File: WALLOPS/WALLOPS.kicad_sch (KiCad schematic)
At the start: 17 parts, among them U9 TPS62147RGXR

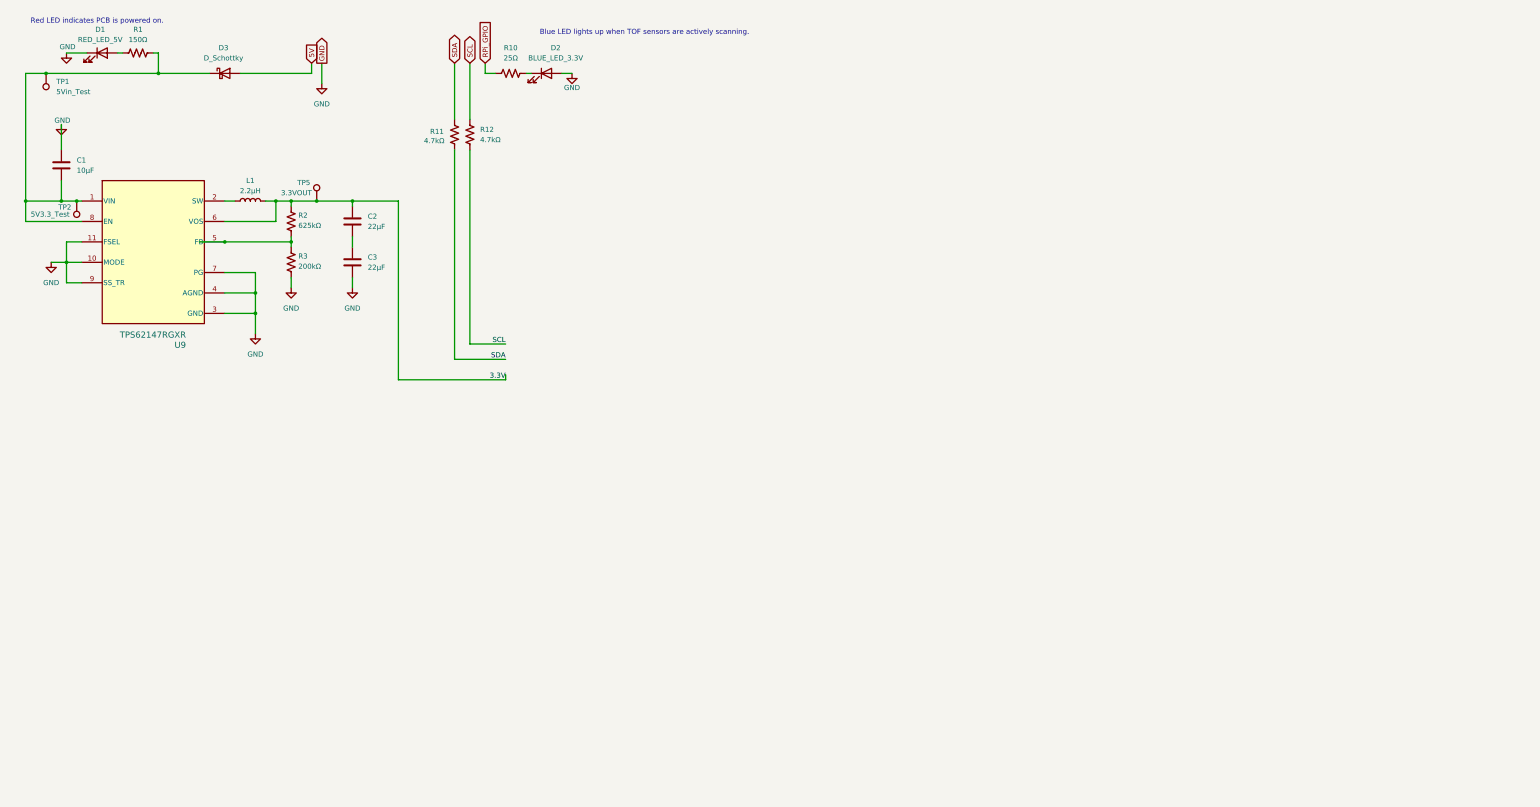
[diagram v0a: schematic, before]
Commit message: Added updated schematics for WALLOPS
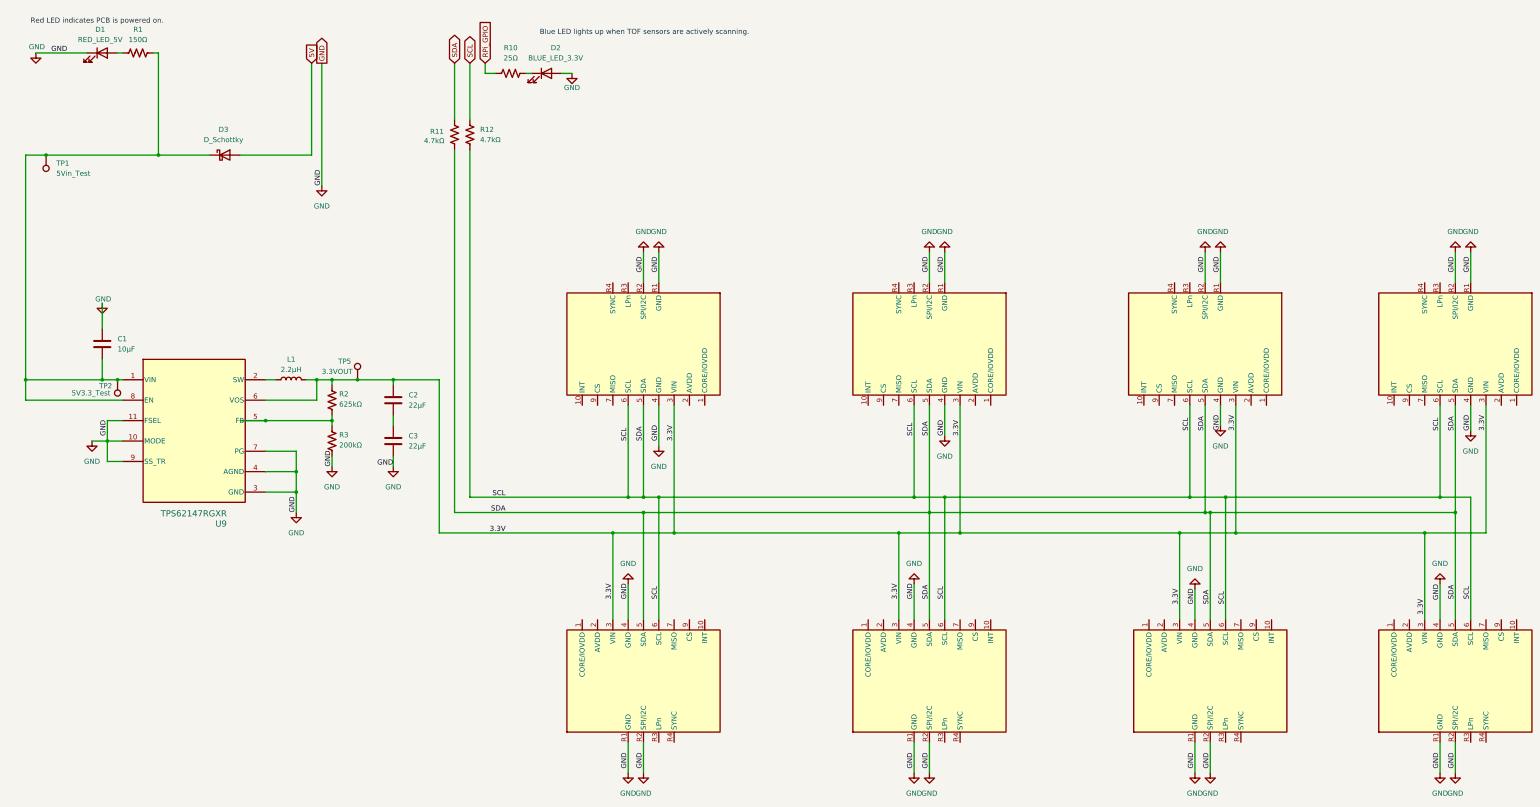
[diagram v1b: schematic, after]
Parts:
- added U1, U2, U3, U4, U5, U6, U7, U8: ~, symbol RockSat_Sym:VL53L8CX
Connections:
- net SDA is gone; now on net SCL: R11.1, R11.2
- net 3.3V: now also U1.3 (VIN), U2.3 (VIN), U3.3 (VIN), U4.3 (VIN), U5.3 (VIN), U6.3 (VIN), U7.3 (VIN), U8.3 (VIN)
- net GND: now also U1.4 (GND), U1.R1 (GND), U1.R2 (SPI/I2C), U2.4 (GND), U2.R1 (GND), U2.R2 (SPI/I2C), U3.4 (GND), U3.R1 (GND), U3.R2 (SPI/I2C), U4.4 (GND), U4.R1 (GND), U4.R2 (SPI/I2C), U5.4 (GND), U5.R1 (GND), U5.R2 (SPI/I2C), U6.4 (GND), U6.R1 (GND), U6.R2 (SPI/I2C), U7.4 (GND), U7.R1 (GND), U7.R2 (SPI/I2C), U8.4 (GND), U8.R1 (GND), U8.R2 (SPI/I2C)
- net SCL: now also U1.5 (SDA), U1.6 (SCL), U2.5 (SDA), U2.6 (SCL), U3.5 (SDA), U3.6 (SCL), U4.5 (SDA), U4.6 (SCL), U5.5 (SDA), U5.6 (SCL), U6.5 (SDA), U6.6 (SCL), U7.5 (SDA), U7.6 (SCL), U8.5 (SDA), U8.6 (SCL)
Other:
- moved on the sheet: C1, C2, C3, D3, L1, R2, R3, TP1, TP2, TP5, U9

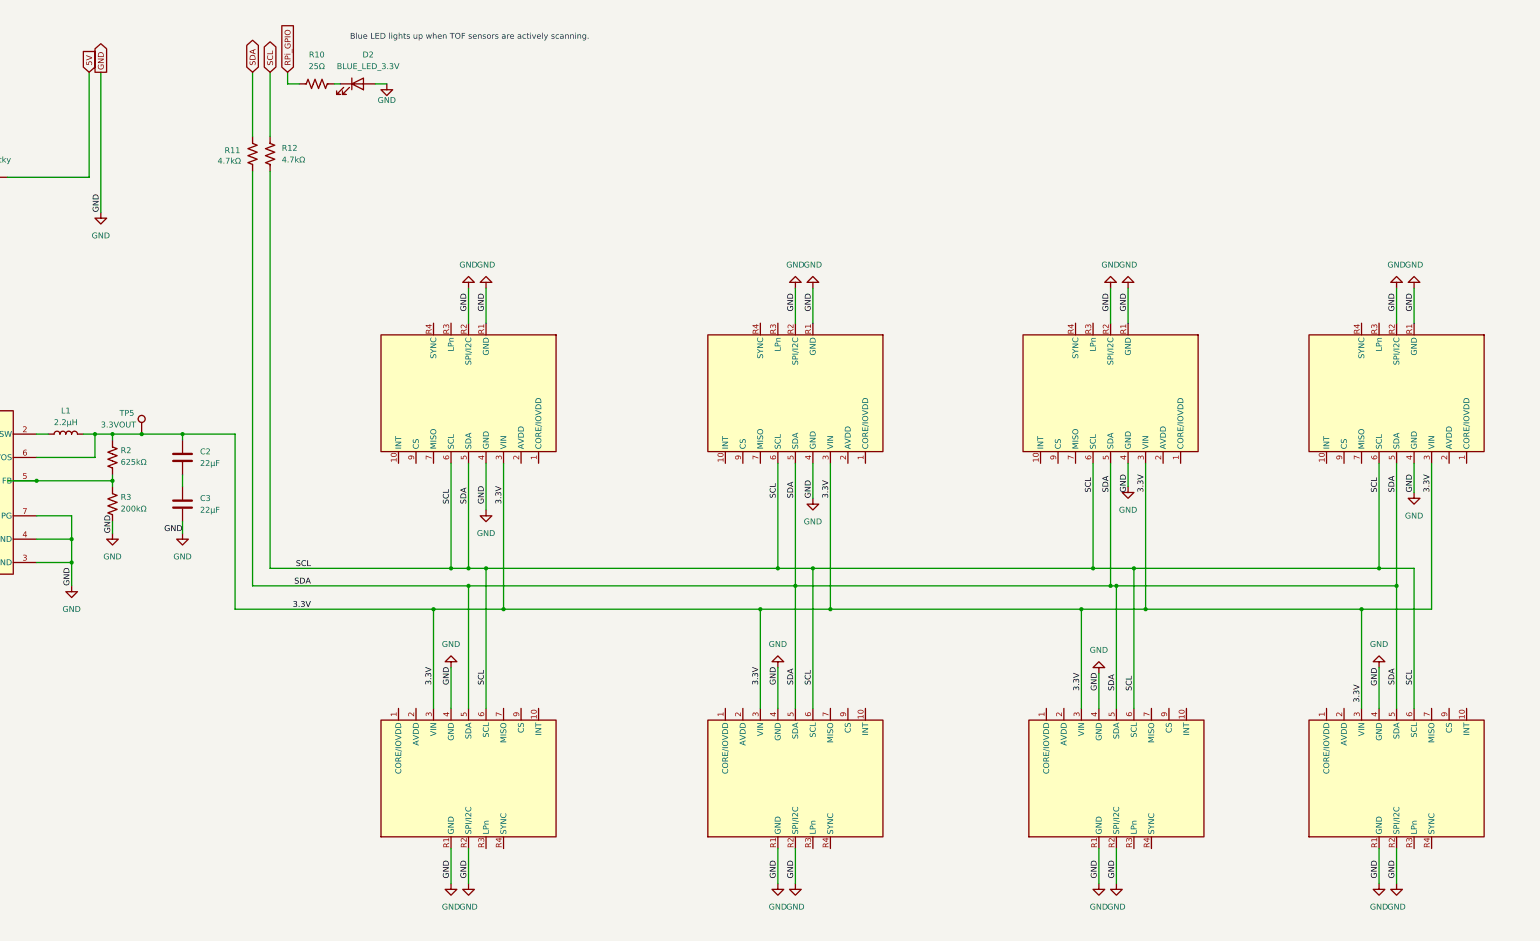
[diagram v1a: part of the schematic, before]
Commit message: Hooked up AVDD to LPn
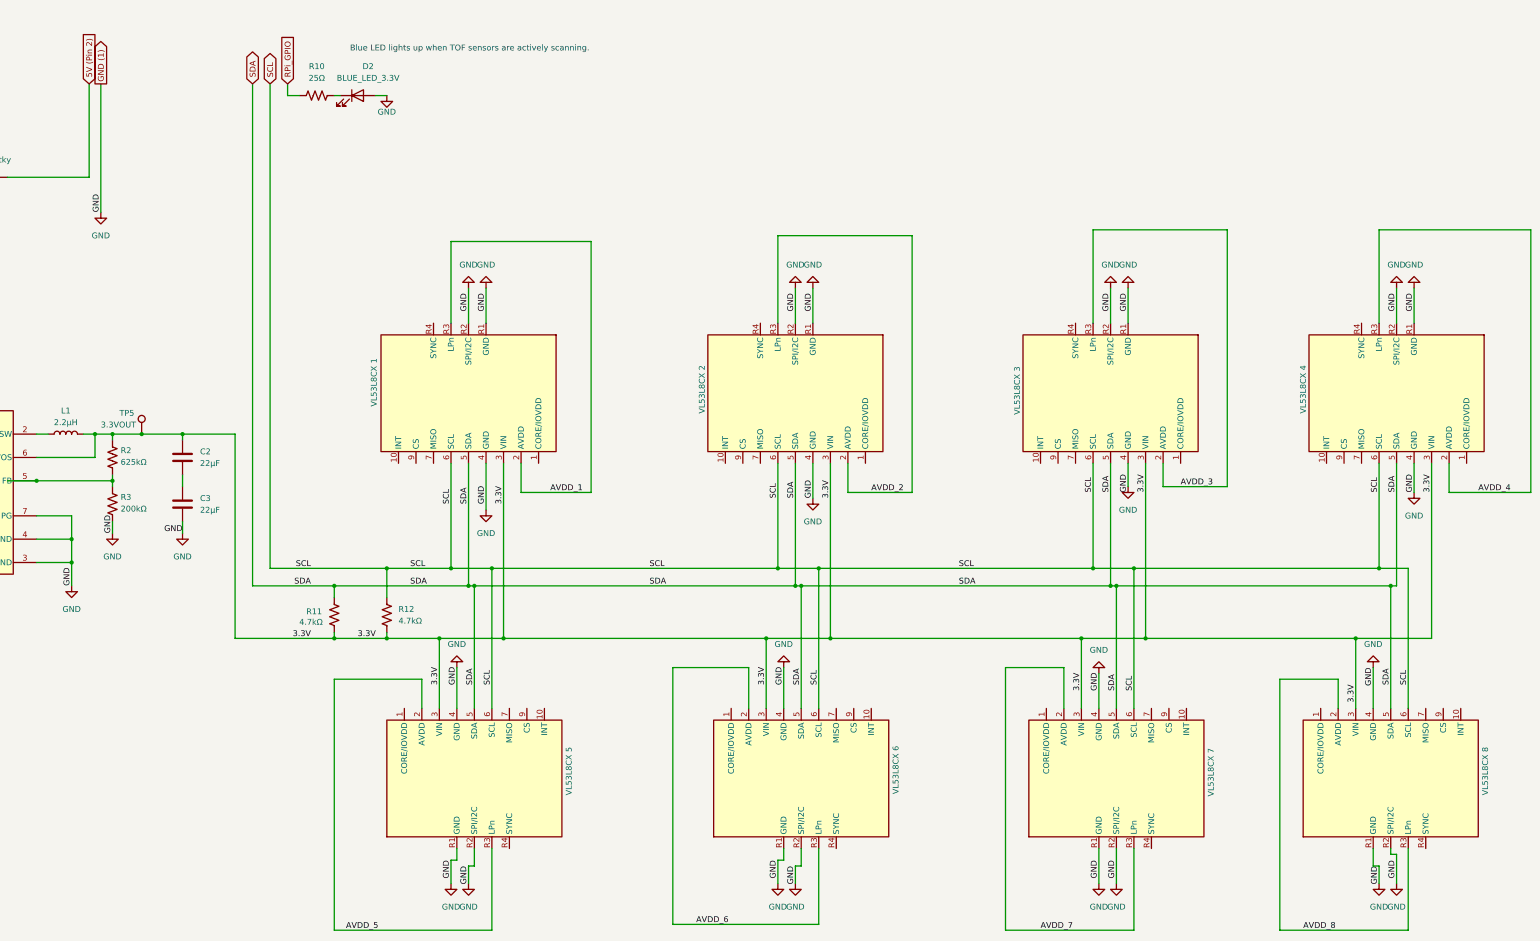
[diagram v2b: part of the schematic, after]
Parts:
- U1: value ~ -> VL53L8CX 4
- U2: value ~ -> VL53L8CX 8
- U3: value ~ -> VL53L8CX 7
- U4: value ~ -> VL53L8CX 5
- U5: value ~ -> VL53L8CX 1
- U6: value ~ -> VL53L8CX 2
- U7: value ~ -> VL53L8CX 3
- U8: value ~ -> VL53L8CX 6
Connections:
- net 3.3V: now also R11.1, R12.1
- net SCL: no longer R11.1, R11.2, R12.1, U1.5 (SDA), U2.5 (SDA), U3.5 (SDA), U4.5 (SDA), U5.5 (SDA), U6.5 (SDA), U7.5 (SDA), U8.5 (SDA)
- net AVDD_8: now reaches U2.2 (AVDD)
- net AVDD_8: now also U2.R3 (LPn)
- net AVDD_4: now reaches U1.2 (AVDD)
- net AVDD_4: now also U1.R3 (LPn)
- net AVDD_2: now reaches U6.2 (AVDD)
- net AVDD_2: now also U6.R3 (LPn)
- net AVDD_6: now reaches U8.2 (AVDD)
- net AVDD_6: now also U8.R3 (LPn)
- net AVDD_5: now reaches U4.2 (AVDD)
- net AVDD_5: now also U4.R3 (LPn)
- net AVDD_1: now reaches U5.2 (AVDD)
- net AVDD_1: now also U5.R3 (LPn)
- net AVDD_3: now reaches U7.2 (AVDD)
- net AVDD_3: now also U7.R3 (LPn)
- net AVDD_7: now reaches U3.2 (AVDD)
- net AVDD_7: now also U3.R3 (LPn)
- net 5V renamed 5V (Pin 2)
- new net SDA: R11.2, U1.5 (SDA), U2.5 (SDA), U3.5 (SDA), U4.5 (SDA), U5.5 (SDA), U6.5 (SDA), U7.5 (SDA), U8.5 (SDA)
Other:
- moved on the sheet: D2, R10, R11, R12

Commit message: Added new 1x9 JST-PH vertical connector from WALLOPS to ML Suite
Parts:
- removed R11, R12: 4.7kΩ, Resistor_SMD:R_0805_2012Metric_Pad1.20x1.40mm_HandSolder, symbol Device:R_US
- removed U1: VL53L8CX 4, symbol RockSat_Sym:VL53L8CX
- removed U2: VL53L8CX 8, symbol RockSat_Sym:VL53L8CX
- removed U3: VL53L8CX 7, symbol RockSat_Sym:VL53L8CX
- removed U4: VL53L8CX 5, symbol RockSat_Sym:VL53L8CX
- removed U5: VL53L8CX 1, symbol RockSat_Sym:VL53L8CX
- removed U6: VL53L8CX 2, symbol RockSat_Sym:VL53L8CX
- removed U7: VL53L8CX 3, symbol RockSat_Sym:VL53L8CX
- removed U8: VL53L8CX 6, symbol RockSat_Sym:VL53L8CX
- added J1: JST-PH 1x8 Connector from WALLOPS to ML Suite, Connector_JST:JST_PH_B9B-PH-K_1x09_P2.00mm_Vertical, symbol Connector:Conn_01x09_Pin
- R10: value 25Ω -> 330Ω
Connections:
- net 5V (Pin 2) is gone; now on net 5Vin: D3.2 (A)
- net GND: now also D2.1 (K), J1.1 (Pin_1); no longer D2.2 (A)
- net SCL: now also J1.3 (Pin_3)
- net SDA: now also J1.4 (Pin_4)
- net 5Vin: now reaches C1.2, D3.1 (K), R1.2, TP1.1, TP2.1, U9.1 (VIN), U9.8 (EN)
- net 5Vin: now also J1.2 (Pin_2)
- net at R10.2: now also D2.2 (A); no longer D2.1 (K)
- net 3.3V renamed 3.3VOUT
- net RPi_GPIO renamed SCAN_LED
- net SCAN_LED: now also J1.5 (Pin_5)
- new net LPn_0: J1.6 (Pin_6)
- new net LPn_1: J1.7 (Pin_7)
- new net LPn_2: J1.8 (Pin_8)
- new net LPn_3: J1.9 (Pin_9)
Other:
- moved on the sheet: C1, C2, C3, D1, D2, D3, L1, R1, R10, R2, R3, TP1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

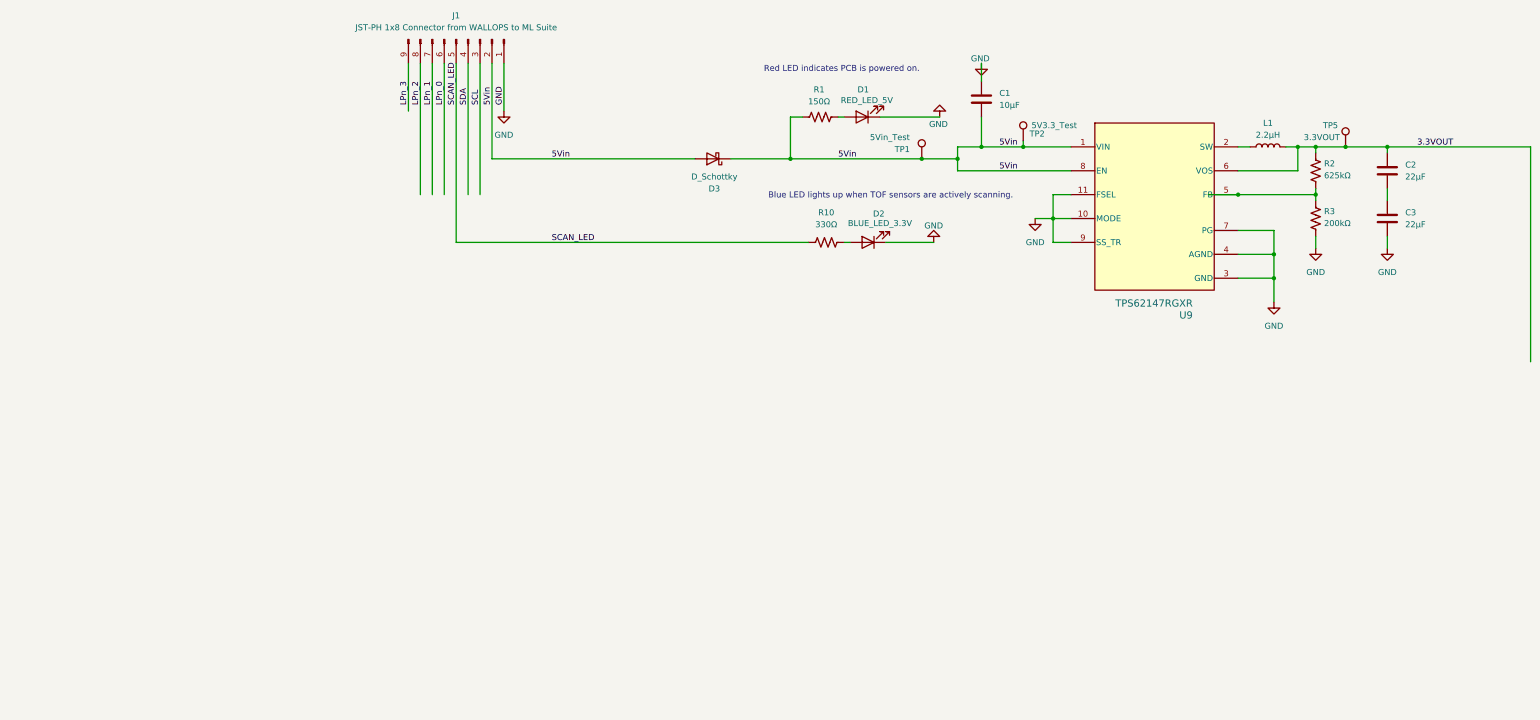
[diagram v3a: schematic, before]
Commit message: Updated schematic and PCB; added symbol, dimensions, and footprint for Pololu VL53L8CX carrier board
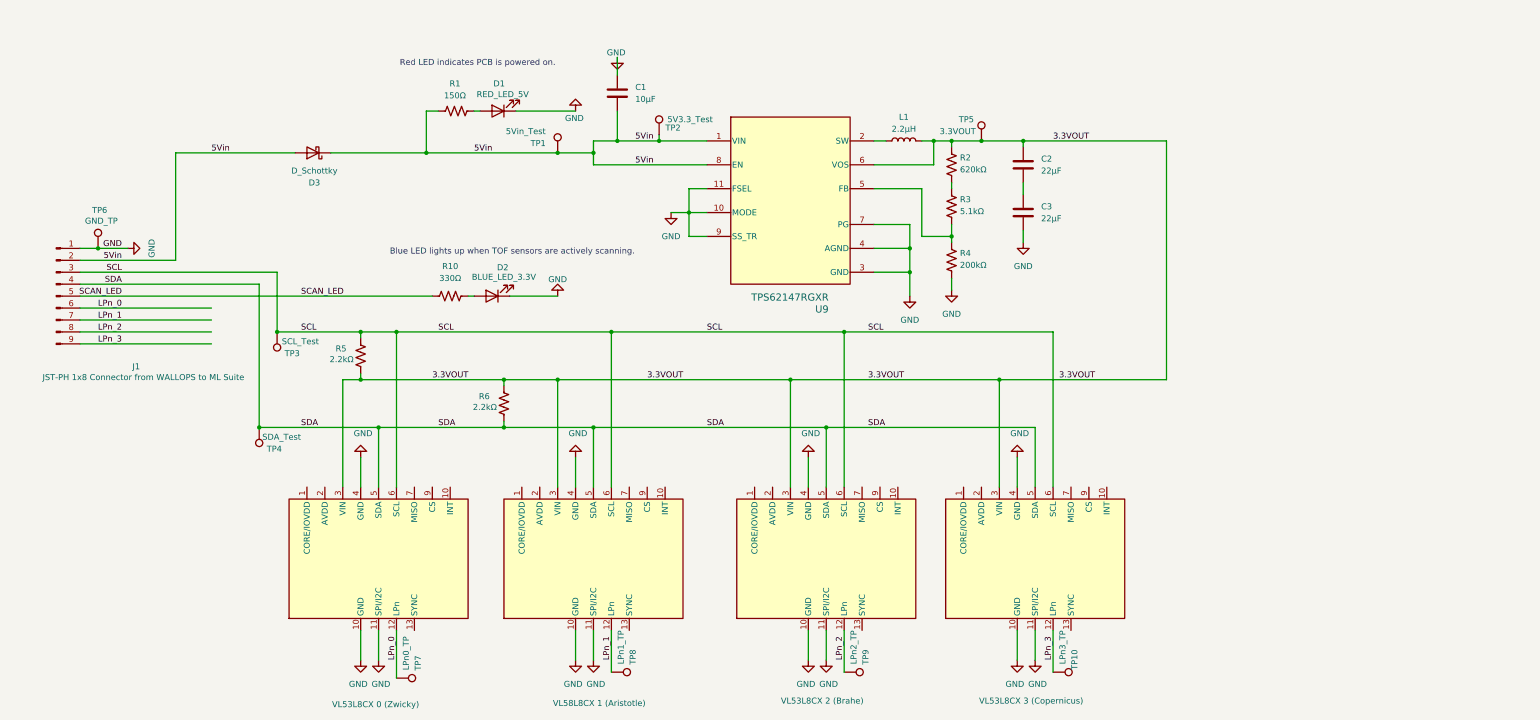
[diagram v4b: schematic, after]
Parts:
- added R3: 5.1kΩ, Resistor_SMD:R_0805_2012Metric_Pad1.20x1.40mm_HandSolder, symbol Device:R_US
- added R5, R6: 2.2kΩ, Resistor_SMD:R_0805_2012Metric_Pad1.20x1.40mm_HandSolder, symbol Device:R_US
- added TP10: LPn3_TP, TestPoint:TestPoint_Pad_D2.0mm, symbol Connector:TestPoint
- added TP3: SCL_Test, TestPoint:TestPoint_Pad_D2.0mm, symbol Connector:TestPoint
- added TP4: SDA_Test, TestPoint:TestPoint_Pad_D2.0mm, symbol Connector:TestPoint
- added TP6: GND_TP, TestPoint:TestPoint_Pad_D2.0mm, symbol Connector:TestPoint
- added TP7: LPn0_TP, TestPoint:TestPoint_Pad_D2.0mm, symbol Connector:TestPoint
- added TP8: LPn1_TP, TestPoint:TestPoint_Pad_D2.0mm, symbol Connector:TestPoint
- added TP9: LPn2_TP, TestPoint:TestPoint_Pad_D2.0mm, symbol Connector:TestPoint
- added U1: VL53L8CX 0 (Zwicky), RockSat:VL53L8CX, symbol RockSat_Sym:VL53L8CX
- added U2: VL58L8CX 1 (Aristotle), RockSat:VL53L8CX, symbol RockSat_Sym:VL53L8CX
- added U3: VL53L8CX 3 (Copernicus), RockSat:VL53L8CX, symbol RockSat_Sym:VL53L8CX
- added U4: VL53L8CX 2 (Brahe), RockSat:VL53L8CX, symbol RockSat_Sym:VL53L8CX
- R2: value 625kΩ -> 620kΩ
- renumbered R3 to R4
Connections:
- net 3.3VOUT: now also R5.2, R6.1, U1.3 (VIN), U2.3 (VIN), U3.3 (VIN), U4.3 (VIN)
- net GND: now also TP6.1, U1.10 (INT), U1.11 (SPI/I2C), U1.4 (GND), U2.10 (INT), U2.11 (SPI/I2C), U2.4 (GND), U3.10 (INT), U3.11 (SPI/I2C), U3.4 (GND), U4.10 (INT), U4.11 (SPI/I2C), U4.4 (GND)
- net LPn_0: now also TP7.1, U1.12 (LPn)
- net LPn_1: now also TP8.1, U2.12 (LPn)
- net LPn_2: now also TP9.1, U4.12 (LPn)
- net LPn_3: now also TP10.1, U3.12 (LPn)
- net SCL: now also R5.1, TP3.1, U1.6 (SCL), U2.6 (SCL), U3.6 (SCL), U4.6 (SCL)
- net SDA: now also R6.2, TP4.1, U1.5 (SDA), U2.5 (SDA), U3.5 (SDA), U4.5 (SDA)
- net at R4.1, U9.5 (FB): now also R3.2; no longer R2.2
- new net: R2.2, R3.1
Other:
- title: WALLOPS 8 Channel LiDAR Scan -> WALLOPS 4x(8x8) Channel LiDAR Scan
- moved on the sheet: C1, C2, C3, D1, D2, D3, J1, L1, R1, R10, R2, R4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
